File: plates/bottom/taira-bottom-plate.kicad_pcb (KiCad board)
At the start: 2 copper layers, 151.5 x 121.2 mm, 8 parts

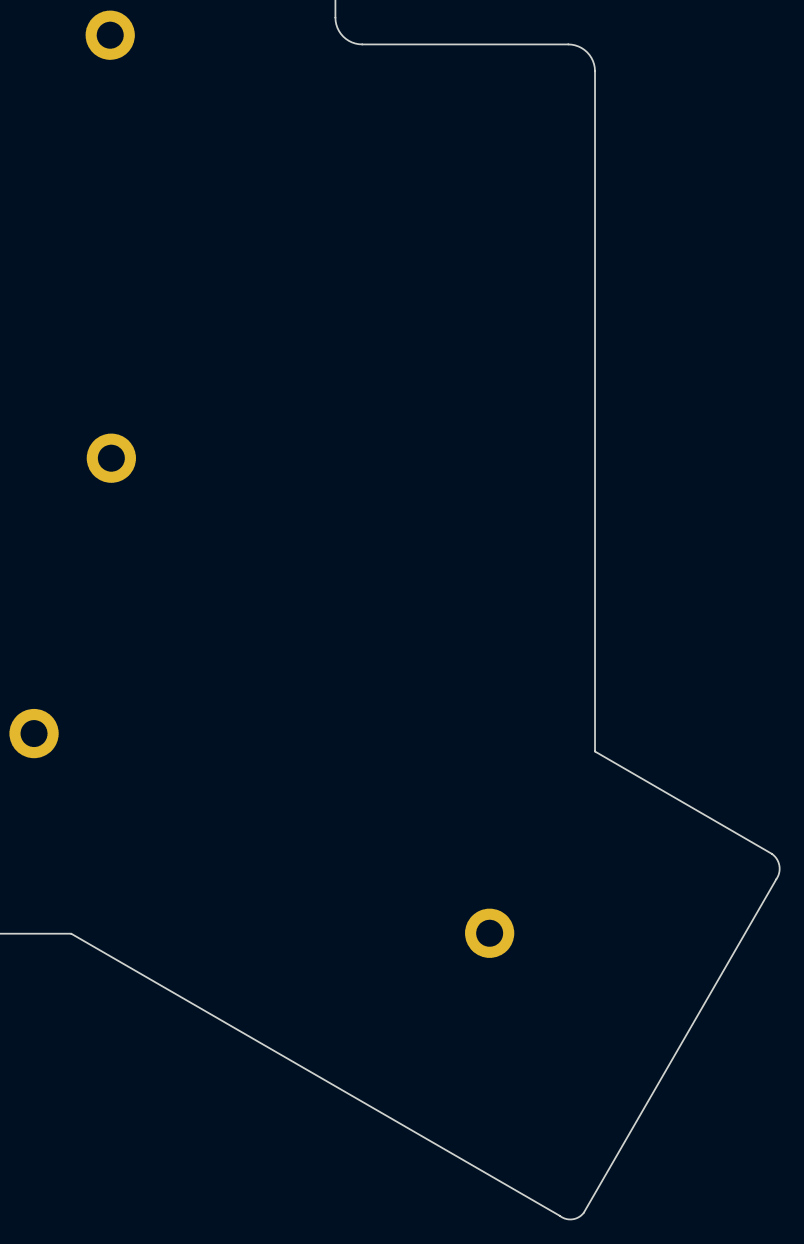
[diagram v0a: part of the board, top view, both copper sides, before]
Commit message: remove outermost two thumb keys (SW32, SW33)
Shrinks the thumb cluster from 5 to 3 keys (SW25, SW30, SW31 remain).
Deletes the footprints, schematic symbols, orphan D32/D33-Pad2 traces,
and the dangling /col6 segments/vias in the cut region; trims Edge.Cuts
on the PCB and both plates to wrap only the remaining keys (H8 stays
enclosed). DRC stays at the pre-existing 4-violation baseline; ERC
clean.

Co-Authored-By: Claude Opus 4.7 <noreply@anthropic.com>
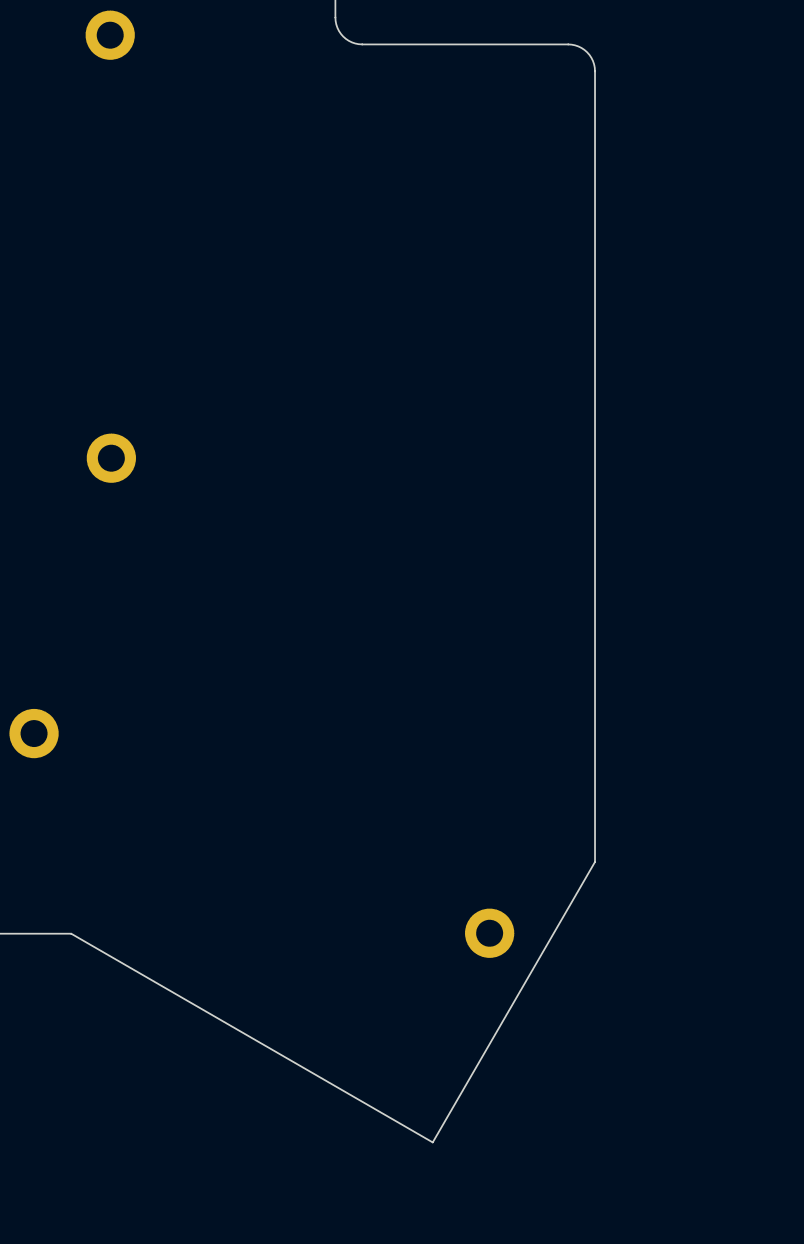
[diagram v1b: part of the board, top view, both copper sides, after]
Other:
- board size 151.5 x 121.2 mm -> 135.8 x 114.6 mm
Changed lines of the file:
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@@
 	(gr_line
 		(start 169.04 134.8)
-		(end 210.699455 158.854935)
+		(end 199.872 152.6)
 		(stroke
 			(width 0.15)
@@
 		(layer "Edge.Cuts")
 	)
-	(gr_arc
-		(start 212.755 158.597)
-		(mid 211.781762 159.16057)
-		(end 210.699455 158.854935)
-		(stroke
-			(width 0.15)
-			(type solid)
-		)
-		(layer "Edge.Cuts")
-	)
 	(gr_line
-		(start 212.755 158.597)
-		(end 229.177 130.151)
+		(start 199.872 152.6)
+		(end 213.71 128.681)
 		(stroke
 			(width 0.15)
@@
 	(gr_line
 		(start 213.71 61.246)
-		(end 213.71 119.261)
+		(end 213.71 128.681)
 		(stroke
 			(width 0.15)
-			(type solid)
-		)
-		(layer "Edge.Cuts")
-	)
-	(gr_line
-		(start 213.71 119.261)
-		(end 228.796 127.992)
-		(stroke
-			(width 0.15)
-			(type solid)
-		)
-		(layer "Edge.Cuts")
-	)
-	(gr_arc
-		(start 228.796 127.992)
-		(mid 229.433644 128.992592)
-		(end 229.177 130.151)
-		(stroke
-			(width 0.15)

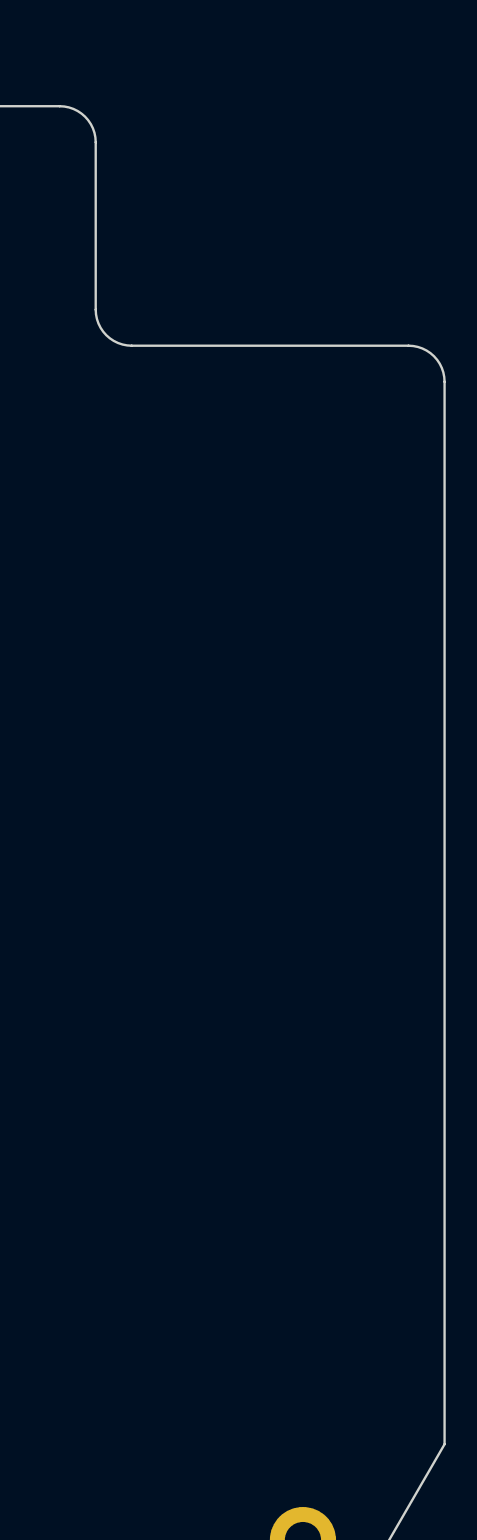
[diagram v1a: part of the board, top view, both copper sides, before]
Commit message: 1.5U bottom thumb + thumb cluster reflow (Pass A)
SW30 enlarged to 1.5U using a new Choc_Hotswap_1.5U footprint (no
stabilizers); the keycap's bottom edges are anchored, so the switch
center shifts up-and-right to (194.515, 133.274). SW31 rotated from
-30° to 180° and placed beside SW29 in the next main-grid column at
(201.295, 106.594). U3 moved up to (204.445, 61.112) so its top edge
aligns with SW26; PCB and both plate Edge.Cuts extended in the
controller area to give U3 the needed vertical room. RSW1, BSW1, BT1
shifted up 15mm to clear the new SW31 and U3 envelopes. Schematic
SW30 footprint property updated to match.

Pass A only: trace endpoints near moved pads have been nudged or, for
SW31's deleted pad stubs, removed. Broader re-routing in KiCad GUI is
pending and will land in a follow-up commit; DRC currently reports
~495 violations in the affected region.

Co-Authored-By: Claude Opus 4.7 <noreply@anthropic.com>
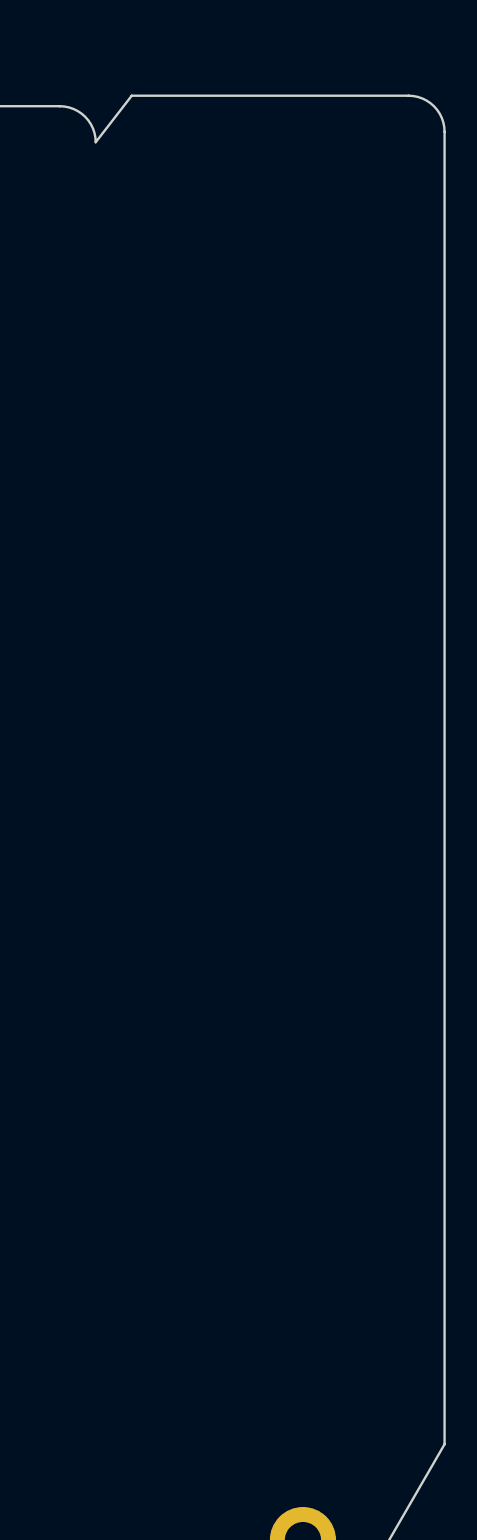
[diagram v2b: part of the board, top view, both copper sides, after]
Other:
- outline, holes or cut-outs redrawn
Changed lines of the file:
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@@
 	)
 	(gr_line
-		(start 191.57 56.674)
-		(end 191.57 46.046)
+		(start 191.57 46.046)
+		(end 193.856 43.094)
+		(stroke
+			(width 0.15)
+			(type solid)
+		)
+		(layer "Edge.Cuts")
+	)
+	(gr_line
+		(start 193.856 43.094)
+		(end 211.424 43.094)
 		(stroke
 			(width 0.15)
@@
 	)
 	(gr_arc
-		(start 193.856 58.96)
-		(mid 192.239554 58.290446)
-		(end 191.57 56.674)
-		(stroke
-			(width 0.15)
-			(type solid)
-		)
-		(layer "Edge.Cuts")
-	)
-	(gr_line
-		(start 193.856 58.96)
-		(end 211.424 58.96)
-		(stroke
-			(width 0.15)
-			(type solid)
-		)
-		(layer "Edge.Cuts")
-	)
-	(gr_arc
-		(start 211.424 58.96)
-		(mid 213.040446 59.629554)
-		(end 213.71 61.246)
+		(start 211.424 43.094)
+		(mid 213.040446 43.763554)
+		(end 213.71 45.38)
 		(stroke
 			(width 0.15)
@@
 	)
 	(gr_line
-		(start 213.71 61.246)
+		(start 213.71 45.38)
 		(end 213.71 128.681)
 		(stroke
